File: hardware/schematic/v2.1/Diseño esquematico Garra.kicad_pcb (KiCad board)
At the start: 2 copper layers, 85.5 x 137 mm, 26 parts

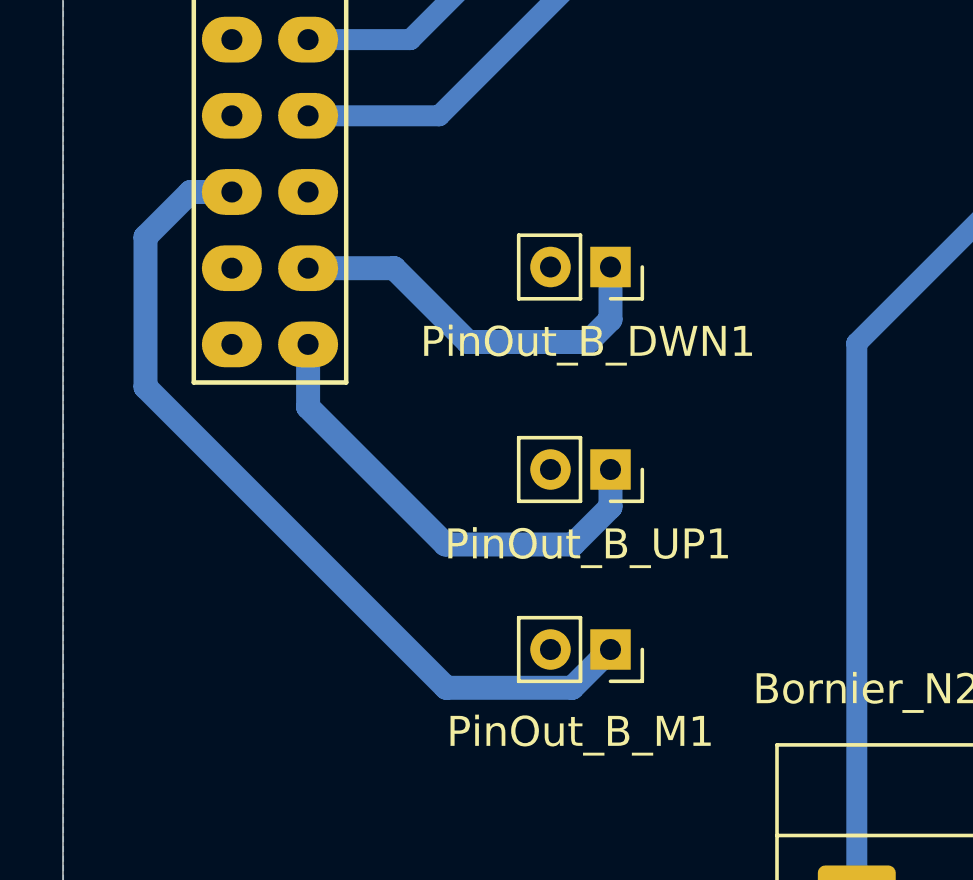
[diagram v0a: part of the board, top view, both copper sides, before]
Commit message: feat: take png and pdf from finished schematic
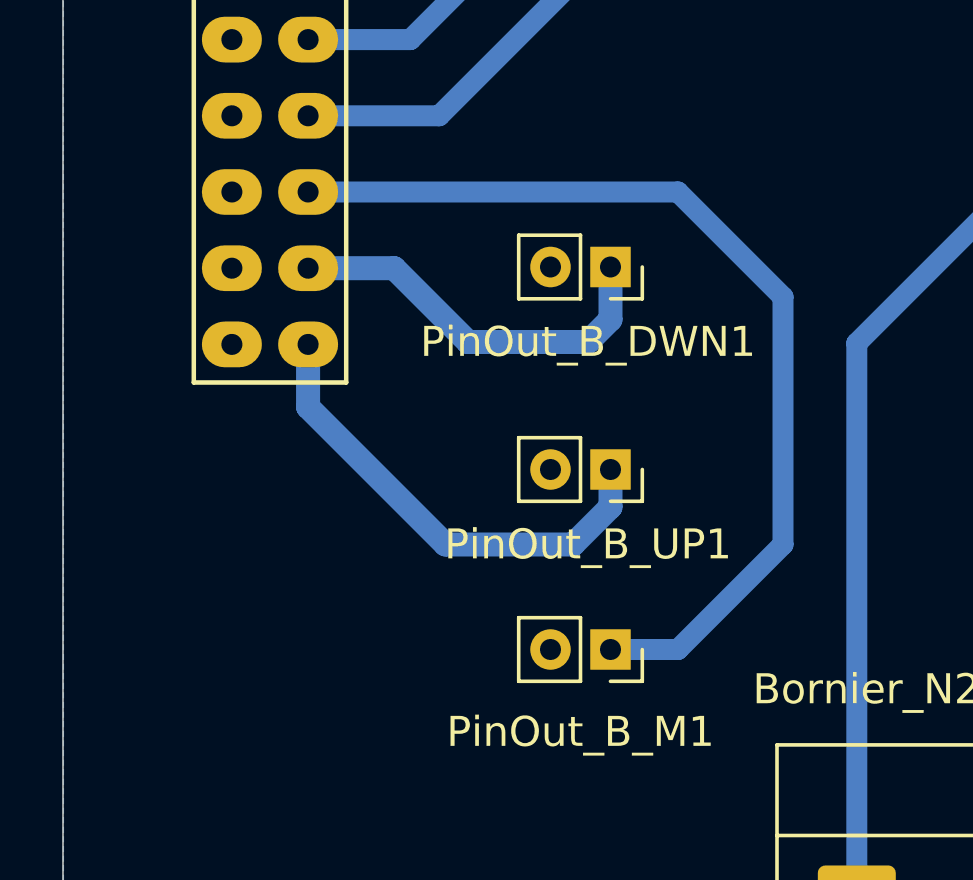
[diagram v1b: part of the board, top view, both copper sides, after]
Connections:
- CIAA-P2 pad 35: B_M -> unconnected-(CIAA-P2-GPIO6-Pad35)
- CIAA-P2 pad 36: unconnected-(CIAA-P2-GPIO5-Pad36) -> B_M
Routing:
- net B_M: track 28.7 -> 32.7 mm
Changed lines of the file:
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@@
 		(grid_origin 35 25)
 		(pcbplotparams
-			(layerselection 0x00000000_00000000_55555555_55555554)
+			(layerselection 0x00000000_00000000_55555555_55555555)
 			(plot_on_all_layers_selection 0x00000000_00000000_00000002_2200888c)
 			(disableapertmacros no)
@@
 	(net 84 "unconnected-(DRV8825_2-~{FLT}-Pad10)")
 	(net 85 "LED")
-	(net 86 "unconnected-(CIAA-P2-GPIO5-Pad36)")
+	(net 86 "unconnected-(CIAA-P2-GPIO6-Pad35)")
 	(footprint ""
 		(layer "F.Cu")
@@
 			(layers "*.Cu" "*.Mask" "F.SilkS")
 			(remove_unused_layers no)
-			(net 67 "B_M")
+			(net 86 "unconnected-(CIAA-P2-GPIO6-Pad35)")
 			(pinfunction "GPIO6")
 			(pintype "passive")
@@
 			(layers "*.Cu" "*.Mask" "F.SilkS")
 			(remove_unused_layers no)
-			(net 86 "unconnected-(CIAA-P2-GPIO5-Pad36)")
+			(net 67 "B_M")
 			(pinfunction "GPIO5")
 			(pintype "passive")
@@
 	)
 	(segment
-		(start 37.75 131.75)
-		(end 39.25 130.25)
-		(width 0.8)
-		(layer "B.Cu")
-		(net 67)
-	)
-	(segment
-		(start 51.974 146.776)
-		(end 47.776 146.776)
-		(width 0.8)
+		(start 55.5 145.5)
+		(end 53.25 145.5)
+		(width 0.7)
 		(layer "B.Cu")
 		(net 67)
 	)
 	(segment
-		(start 37.75 136.75)
-		(end 37.75 131.75)
-		(width 0.8)
+		(start 59 142)
+		(end 55.5 145.5)
+		(width 0.7)
 		(layer "B.Cu")
 		(net 67)
 	)
 	(segment
-		(start 47.776 146.776)
-		(end 37.75 136.75)
-		(width 0.8)
+		(start 43.17 130.25)
+		(end 55.5 130.25)
+		(width 0.7)
 		(layer "B.Cu")
 		(net 67)
 	)
 	(segment
-		(start 39.25 130.25)
-		(end 40.63 130.25)
-		(width 0.8)
+		(start 59 133.75)
+		(end 59 142)
+		(width 0.7)
 		(layer "B.Cu")
 		(net 67)
 	)
 	(segment
-		(start 53.25 145.5)
-		(end 51.974 146.776)
-		(width 0.8)
+		(start 55.5 130.25)
+		(end 59 133.75)
+		(width 0.7)
 		(layer "B.Cu")
 		(net 67)

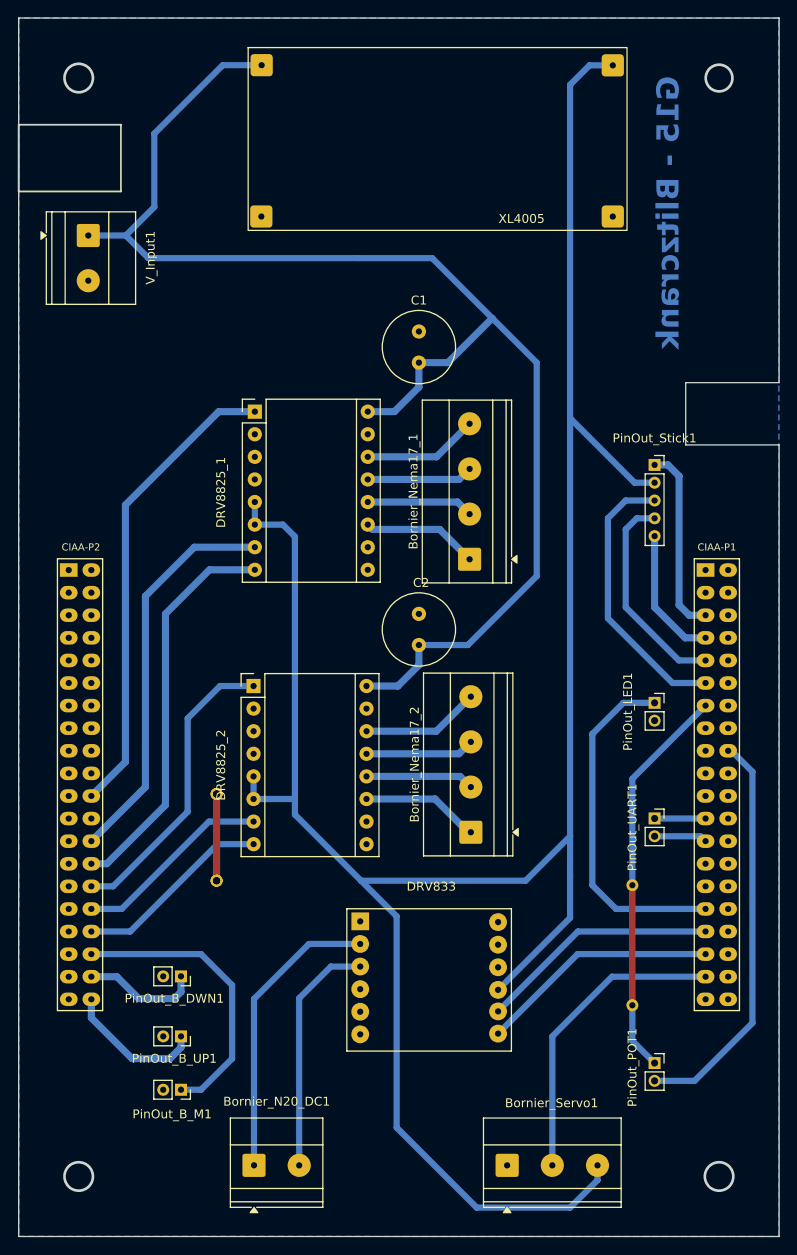
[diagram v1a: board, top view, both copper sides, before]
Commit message: feat: valid pdf PCB template
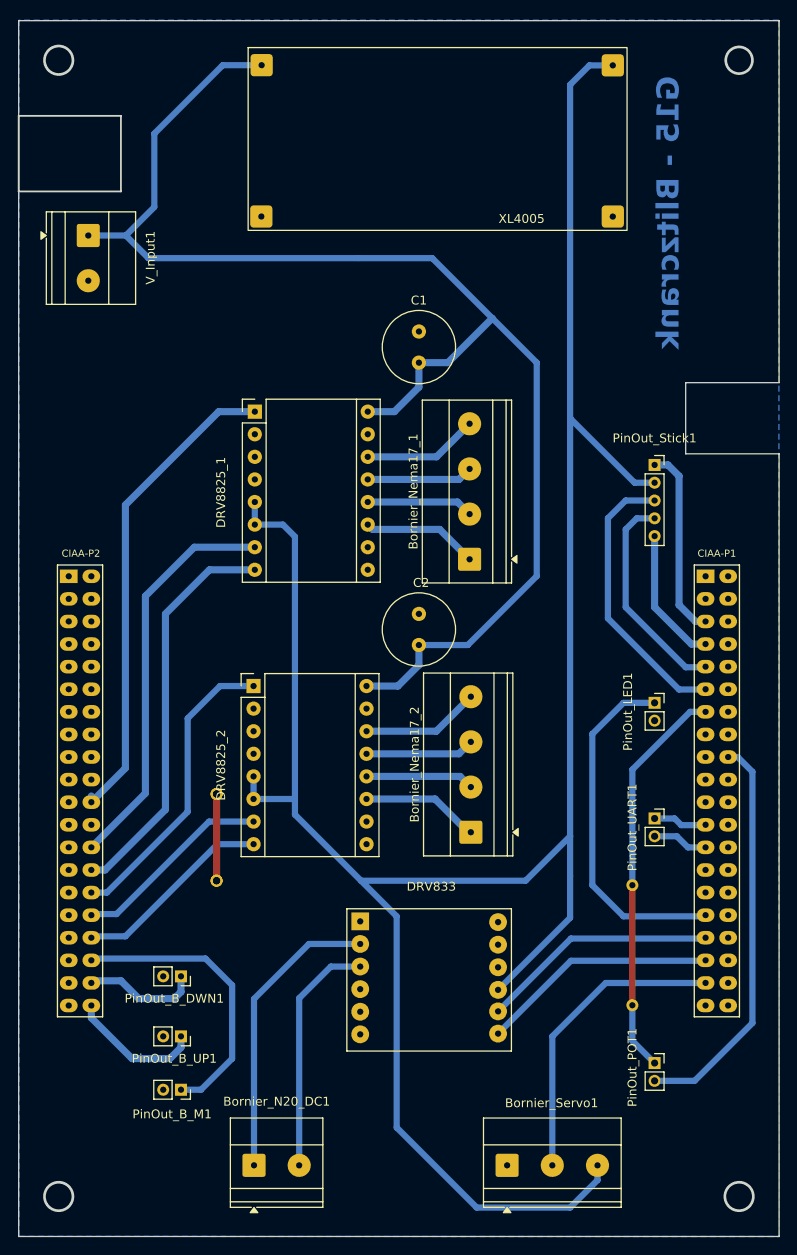
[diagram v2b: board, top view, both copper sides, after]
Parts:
- moved CIAA-P1 0.70 mm to (113.5, 111.9)
- moved CIAA-P2 0.70 mm to (41.9, 111.9)
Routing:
- net EN1: track 53.2 -> 54.6 mm
- net STEP1: track 44.6 -> 45.3 mm
- net B_UP: track 16.2 -> 15.5 mm
- net DIR1: track 44.7 -> 45.2 mm
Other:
- board size 85.5 x 137 mm -> 85.5 x 136.7 mm

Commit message: fix: Expand PCB routes and copper holes
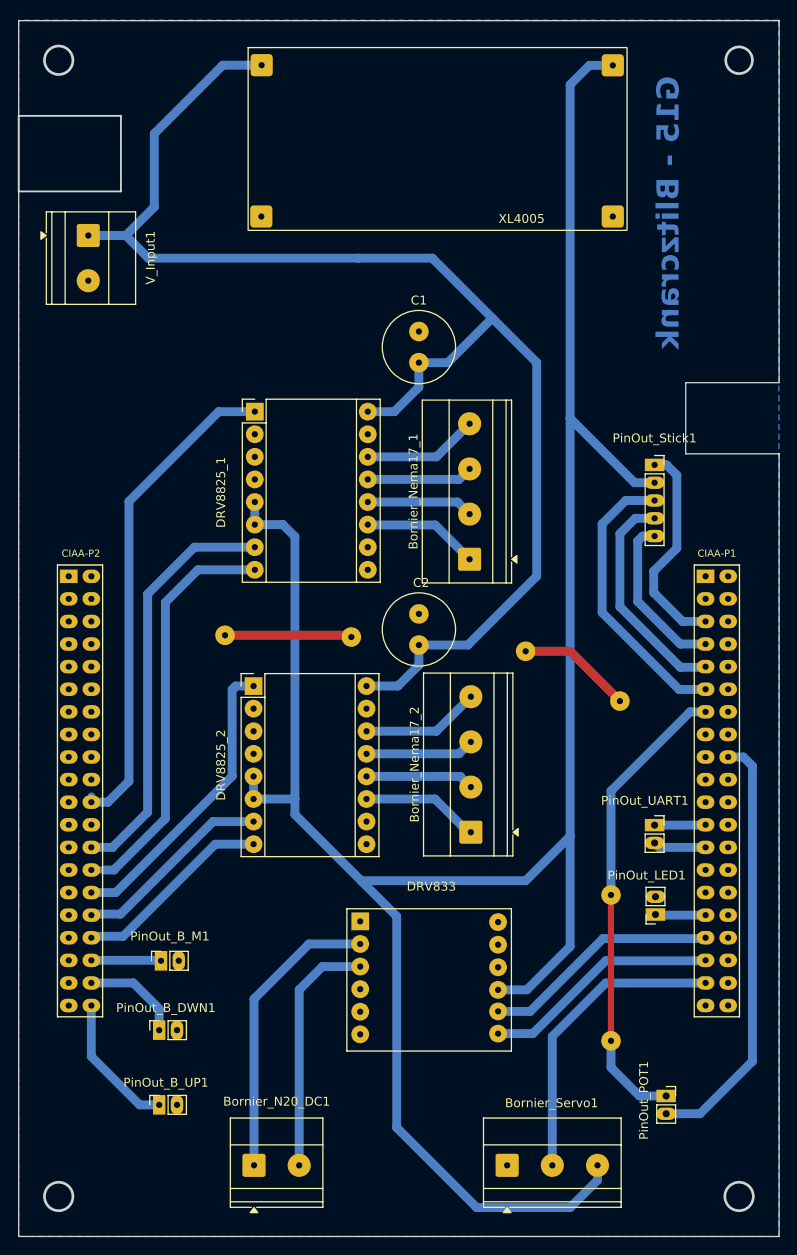
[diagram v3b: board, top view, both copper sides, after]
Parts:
- removed the ? at (57.2, 122.0) (x2)
- removed the ? at (57.2, 112.2) (x2)
- added ?: , , F.Cu at (72.4, 94.6)
- added ?: , , F.Cu at (92.0, 96.2)
- added ?: , , F.Cu at (102.6, 101.8)
- added ?: , , F.Cu at (58.2, 94.4)
- moved PinOut_LED1 23.8 mm to (106.6, 125.8), turned to 180 degrees
- moved PinOut_B_M1 14.7 mm to (51.0, 131.0), turned to 90 degrees
- moved PinOut_B_UP1 8.08 mm to (50.8, 147.2), turned to 90 degrees
- moved PinOut_B_DWN1 6.53 mm to (50.8, 138.8), turned to 90 degrees
- moved ? 4.66 mm to (101.6, 140.0)
- moved PinOut_POT1 3.92 mm to (107.8, 146.2)
- moved ? 2.64 mm to (101.6, 123.6)
- moved PinOut_UART1 0.75 mm to (106.5, 115.8)
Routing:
- net LED: track 39.7 -> 5.84 mm
- net B_M: track 32.6 -> 8.13 mm
- net GND: track 9.75 -> 27.2 mm
- net POT: track 45.0 -> 52.7 mm
- net GND_POT: track 45.4 -> 48.5 mm
- net GND_Stick: track 15.4 -> 18.5 mm
- net Stick_ON: track 21.5 -> 24.4 mm
- net 5V: track 263.6 -> 265.5 mm
- net STEP1: track 45.3 -> 46.7 mm
- net DIR1: track 45.2 -> 46.6 mm
- net B_DWN: track 13.1 -> 11.7 mm
- net EN1: track 54.6 -> 55.7 mm
- net VRY: track 24.3 -> 25.3 mm
- net MOTOR_GND: track 27.1 -> 27.7 mm
- net VRX: track 31.1 -> 31.7 mm
